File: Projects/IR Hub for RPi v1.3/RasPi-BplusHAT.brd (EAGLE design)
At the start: 65 x 56 mm, 37 parts, among them SW1 SPST_TACT-KMR2, SW2 SPST_TACT-KMR2, SW3 SPST_TACT-KMR2, T1 2N4401, T2 2N4401, T3 2N4401, T4 2N4401

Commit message: Revert "Revert "relocated IRRCV""
This reverts commit e9af4263ddd1cfc11cb1365f6dffa75911e4cf46.
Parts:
- added U$1, U$2: 74HC2G17-Q100, varshneya:SC-70-6L
- RUN: value (none) -> RST
- moved LED1-IR 25.2 mm to (8.00, 21.5)
- moved LED2-IR 25.2 mm to (8.00, 34.5)
- moved IRRCV 12.9 mm to (3.50, 12.5), turned to 270 degrees
- moved LED8-IR-RCV 10.1 mm to (13.5, 8.50), turned to 90 degrees
- moved R10 8.32 mm to (22.0, 4.00), turned to 180 degrees
- moved R8 7.16 mm to (13.5, 4.00), turned to 180 degrees
- moved T4 4.27 mm to (22.0, 14.0), turned to 180 degrees
- moved T3 4.00 mm to (15.0, 14.0), turned to 180 degrees
- moved T2 2.92 mm to (22.0, 27.0), turned to 0 degrees
- moved R11 2.69 mm to (22.0, 8.50), turned to 0 degrees
- moved R1 2.55 mm to (23.5, 35.0)
- moved R2 2.55 mm to (12.5, 35.0)
- moved R3 2.55 mm to (18.0, 35.0)
- moved C1 2.50 mm to (34.5, 12.0)
- moved R12 2.50 mm to (34.5, 20.0)
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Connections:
- new net N$12: C2.1, R13.1, SW2.1, SW2.3, U$1.3
- new net N$13: C3.1, R14.1, R15.1, U$2.3
- new net N$9: C1.1, R12.1, SW1.2, SW1.4, U$1.1
- net +3V3: now also U$1.5, U$2.5
- net GND: now also U$1.2, U$2.2
- net GPIO17: now also U$1.6; no longer C1.1, R12.1, SW1.2, SW1.4
- net GPIO27: now also U$1.4; no longer C2.1, R13.1, SW2.1, SW2.3
- net RST: now also U$2.4; no longer C3.1, R14.1, R15.1
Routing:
- net N$3: track 46.8 -> 10.2 mm
- net GPIO27: track 56.0 -> 29.2 mm
- net N$12: track 0.00 -> 26.4 mm, vias 0 -> 2
- net GPIO17: track 54.1 -> 29.7 mm
- net N$9: track 0.00 -> 23.4 mm, vias 0 -> 2
- net N$13: track 0.00 -> 17.7 mm
- net RST: track 67.3 -> 52.5 mm
- net +3V3: track 86.1 -> 100.4 mm
- net N$2: track 13.7 -> 27.5 mm
- net N$6: track 13.6 -> 24.9 mm
- net N$4: track 31.2 -> 22.5 mm
- net GPIO22: track 14.1 -> 22.7 mm, vias 2 -> 1
- net N$10: track 22.8 -> 15.6 mm
- net N$23: track 5.73 -> 12.3 mm
- net +5V: track 118.3 -> 124.3 mm
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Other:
- board text added: "HA Hub v1.3 July 2015"
- board text added: "Home Automation Hub v1.3"
- board text added: "Open Qbit Systems"
- board text added: "TODO 1. Check the Schmitt debouncing on breadboard 2. check the polarity of the IR LEDs 3. Check both ICs wrt 74HC/74LV/... for 3.3V DONE 1. Add schmitt buffers for all the push buttons (create part) 2. ELIMINATED - Verify the Watchdog circuit 3. ELIMINATED - Will RPi gpio go in a state to allow disabling WD? 4. Ensure long push for RESET push button (cap and resistor values) 5. Move Power LED to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"
- board text added: "openqbitsystems.blogspot.com"
- board text added: "|X>"
- board text removed: "HA Hub v3.0 July 10, 2015"
- board text removed: "Home Automation Hub v3.0"
- board text removed: "Qbit Devices"
- board text removed: "QbitDevices.wordpress.com"
- board text removed: "TODO 1. Add schmitt buffers for all the push buttons 2. check the polarity of the IR LEDs 3. Check both ICs wrt 74HC/74LV/... for 3.3V DONE 1. ELIMINATED - Verify the Watchdog circuit 2. ELIMINATED - Will RPi gpio go in a state to allow disabling WD? 3. Ensure long push for RESET push button (cap and resistor values) 4. Move Power LED to the Status LEDs area 5. check RUN location 6. Verify the IR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"
- board text removed: "|x>"

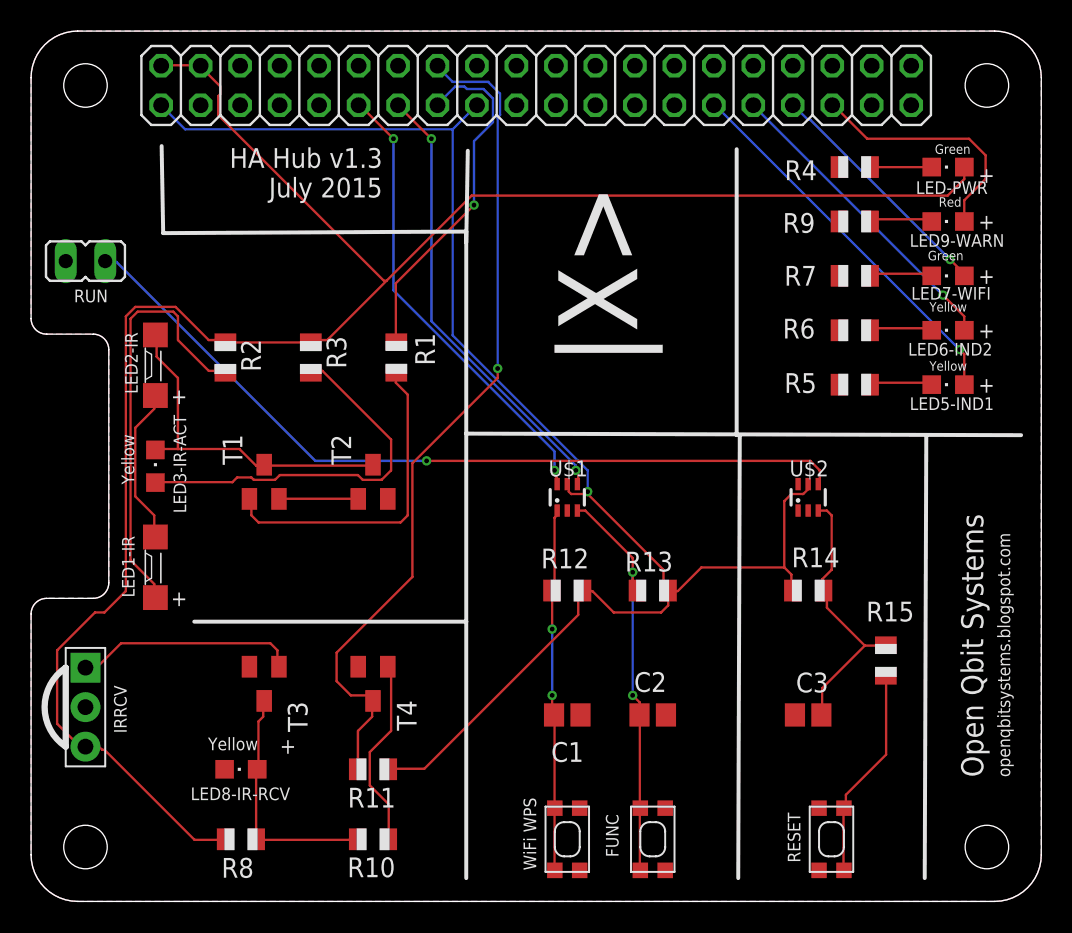
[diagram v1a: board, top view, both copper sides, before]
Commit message: minor teaks to silk, changed one LED to blue color
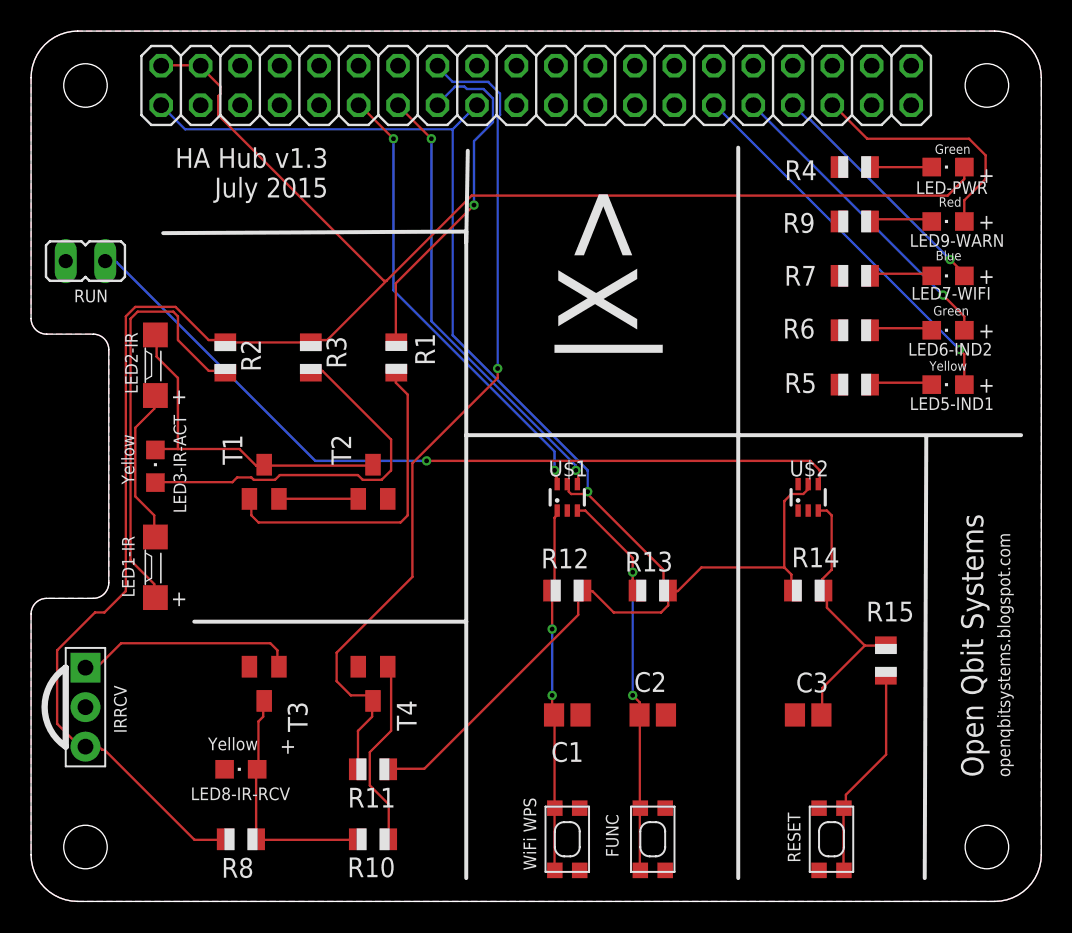
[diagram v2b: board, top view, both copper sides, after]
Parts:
- LED6-IND2: value Yellow -> Green
- LED7-WIFI: value Green -> Blue
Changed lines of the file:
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@@
 <circle x="61.5" y="52.5" radius="1.55" width="3.1" layer="42"/>
 <text x="61.27" y="7.99" size="1.4224" layer="25" rot="R90">Open Qbit Systems</text>
-<text x="22.61" y="48.47" size="1.27" layer="25" rot="R180">HA Hub v1.3
+<text x="19.11" y="48.47" size="1.27" layer="25" rot="R180">HA Hub v1.3
 July 2015</text>
 <wire x1="10.5" y1="18" x2="28" y2="18" width="0.254" layer="25"/>
-<wire x1="28" y1="43.1" x2="28" y2="30.1" width="0.254" layer="25"/>
-<wire x1="28" y1="30.1" x2="28" y2="18" width="0.254" layer="25"/>
+<wire x1="28" y1="43.1" x2="28" y2="30" width="0.254" layer="25"/>
+<wire x1="28" y1="30" x2="28" y2="18" width="0.254" layer="25"/>
 <wire x1="28" y1="18" x2="28" y2="1.5" width="0.254" layer="25"/>
 <wire x1="28" y1="43.1" x2="8.5" y2="43" width="0.254" layer="25"/>
@@
 <text x="32.5" y="2" size="0.8128" layer="25" rot="R90">WiFi WPS</text>
 <wire x1="28.1" y1="48.3" x2="28" y2="42.4" width="0.254" layer="25"/>
-<wire x1="45.4" y1="48.4" x2="45.4" y2="30" width="0.254" layer="25"/>
-<wire x1="63.7" y1="30" x2="28" y2="30.1" width="0.254" layer="25"/>
+<wire x1="45.5" y1="48.5" x2="45.5" y2="30" width="0.254" layer="25"/>
+<wire x1="63.7" y1="30" x2="28" y2="30" width="0.254" layer="25"/>
 <text x="-48.2222" y="19.964" size="1.016" layer="48">
 TODO
@@
 <text x="62" y="47.25" size="1.016" layer="21" rot="R180">+</text>
 <text x="16" y="9.5" size="1.016" layer="21">+</text>
-<wire x1="45.6" y1="29.9" x2="45.5" y2="1.5" width="0.254" layer="25"/>
+<wire x1="45.5" y1="29.9" x2="45.5" y2="1.5" width="0.254" layer="25"/>
 <text x="60" y="17" size="2.54" layer="26" rot="MR0">Open Qbit Systems</text>
 <text x="60" y="12.5" size="1.9304" layer="26" rot="MR0">openqbitsystems.blogspot.com</text>
@@
 <text x="63" y="8" size="0.8128" layer="25" rot="R90">openqbitsystems.blogspot.com</text>
 <text x="60" y="42" size="2.1844" layer="26" rot="MR0">Home Automation Hub v1.3</text>
-<wire x1="8.4" y1="48.6" x2="8.5" y2="43" width="0.254" layer="25"/>
 </plain>
 <attributes>
@@
 <attribute name="MPN" value="CRCW0805100RFKEA" x="53" y="33.25" size="1.778" layer="27" display="off"/>
 </element>
-<element name="LED6-IND2" library="led" package="CHIPLED_0805" value="Yellow" x="59" y="36.75" smashed="yes" rot="R90">
+<element name="LED6-IND2" library="led" package="CHIPLED_0805" value="Green" x="59" y="36.75" smashed="yes" rot="R90">
 <attribute name="NAME" x="56.43" y="35.12" size="0.8128" layer="25"/>
-<attribute name="VALUE" x="57.8" y="37.95" size="0.6096" layer="25"/>
-<attribute name="OC_NEWARK" value="95W3804" x="59" y="36.75" size="1.778" layer="27" rot="R90" display="off"/>
+<attribute name="VALUE" x="58.05" y="37.7" size="0.6096" layer="25"/>
+<attribute name="OC_NEWARK" value="95W3800" x="59" y="36.75" size="1.778" layer="27" rot="R90" display="off"/>
 <attribute name="MF" value="" x="59" y="36.75" size="1.778" layer="27" rot="R90" display="off"/>
-<attribute name="MPN" value="150080YS75000" x="59" y="36.75" size="1.778" layer="27" rot="R90" display="off"/>
+<attribute name="MPN" value="150080GS75000" x="59" y="36.75" size="1.778" layer="27" rot="R90" display="off"/>
 </element>
 <element name="R6" library="adafruit" package="R0805" value="100Ohm" x="53" y="36.75" smashed="yes">
@@
 <attribute name="MPN" value="CRCW0805100RFKEA" x="53" y="43.75" size="1.778" layer="27" display="off"/>
 </element>
-<element name="LED7-WIFI" library="led" package="CHIPLED_0805" value="Green" x="59" y="40.25" smashed="yes" rot="R90">
+<element name="LED7-WIFI" library="led" package="CHIPLED_0805" value="Blue" x="59" y="40.25" smashed="yes" rot="R90">
 <attribute name="NAME" x="56.63" y="38.72" size="0.8128" layer="25"/>
-<attribute name="VALUE" x="57.7" y="41.25" size="0.6096" layer="25"/>
-<attribute name="OC_NEWARK" value="95W3800" x="59" y="40.25" size="1.778" layer="27" rot="R90" display="off"/>
+<attribute name="VALUE" x="58.2" y="41.25" size="0.6096" layer="25"/>
+<attribute name="OC_NEWARK" value="95W3799" x="59" y="40.25" size="1.778" layer="27" rot="R90" display="off"/>
 <attribute name="MF" value="" x="59" y="40.25" size="1.778" layer="27" rot="R90" display="off"/>
-<attribute name="MPN" value="150080GS75000" x="59" y="40.25" size="1.778" layer="27" rot="R90" display="off"/>
+<attribute name="MPN" value="150080BS75000" x="59" y="40.25" size="1.778" layer="27" rot="R90" display="off"/>
 </element>
 <element name="R7" library="adafruit" package="R0805" value="100Ohm" x="53" y="40.25" smashed="yes">
@@
 <element name="R14" library="adafruit" package="R0805" value="1M" x="50" y="20" smashed="yes" rot="R180">
 <attribute name="MF" value="VISHAY/DALE" x="50" y="20" size="1.778" layer="27" rot="R180" display="off"/>
-<attribute name="MPN" value="CRCW080510K0FKEA" x="50" y="20" size="1.778" layer="27" rot="R180" display="off"/>
-<attribute name="OC_NEWARK" value="52K9795" x="50" y="20" size="1.778" layer="27" rot="R180" display="off"/>
+<attribute name="MPN" value="CRCW08051M00FKEA" x="50" y="20" size="1.778" layer="27" rot="R180" display="off"/>
+<attribute name="OC_NEWARK" value="52K9759" x="50" y="20" size="1.778" layer="27" rot="R180" display="off"/>
 <attribute name="NAME" x="48.938" y="21.5" size="1.27" layer="25"/>
 </element>
@@
 </element>
 <element name="R15" library="adafruit" package="R0805" value="100K" x="55" y="15.5" smashed="yes" rot="R270">
-<attribute name="OC_NEWARK" value="52K9795" x="55" y="15.5" size="1.016" layer="27" rot="R270" display="off"/>
+<attribute name="OC_NEWARK" value="52K9808" x="55" y="15.5" size="1.016" layer="27" rot="R270" display="off"/>
 <attribute name="MF" value="VISHAY/DALE" x="55" y="15.5" size="1.016" layer="27" rot="R270" display="off"/>
-<attribute name="MPN" value="CRCW080510K0FKEA" x="55" y="15.5" size="1.016" layer="27" rot="R270" display="off"/>
+<attribute name="MPN" value="CRCW0805100KFKEA" x="55" y="15.5" size="1.016" layer="27" rot="R270" display="off"/>
 <attribute name="NAME" x="53.738" y="18.016" size="1.27" layer="25"/>
 </element>
 <element name="U$1" library="varshneya" package="SC-70-6L" value="74HC2G17-Q100" x="34.5" y="26" smashed="yes">
 <attribute name="NAME" x="33.3" y="27.35" size="1.016" layer="25"/>
+<attribute name="OC_NEWARK" value="71R2196" x="34.5" y="26" size="1.778" layer="27" display="off"/>
+<attribute name="MF" value="" x="34.5" y="26" size="1.778" layer="27" display="off"/>
+<attribute name="MPN" value="74HC2G17GW,125" x="34.5" y="26" size="1.778" layer="27" display="off"/>
 </element>
 <element name="U$2" library="varshneya" package="SC-70-6L" value="74HC2G17-Q100" x="50" y="26" smashed="yes">
 <attribute name="NAME" x="48.8" y="27.35" size="1.016" layer="25"/>
+<attribute name="OC_NEWARK" value="71R2196" x="50" y="26" size="1.778" layer="27" display="off"/>
+<attribute name="MF" value="" x="50" y="26" size="1.778" layer="27" display="off"/>
+<attribute name="MPN" value="74HC2G17GW,125" x="50" y="26" size="1.778" layer="27" display="off"/>
 </element>
 </elements>

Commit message: near final version - checkpoint
Pending AIs -
check polarity of the IR LEDs
check the buffer circuit on breadboard
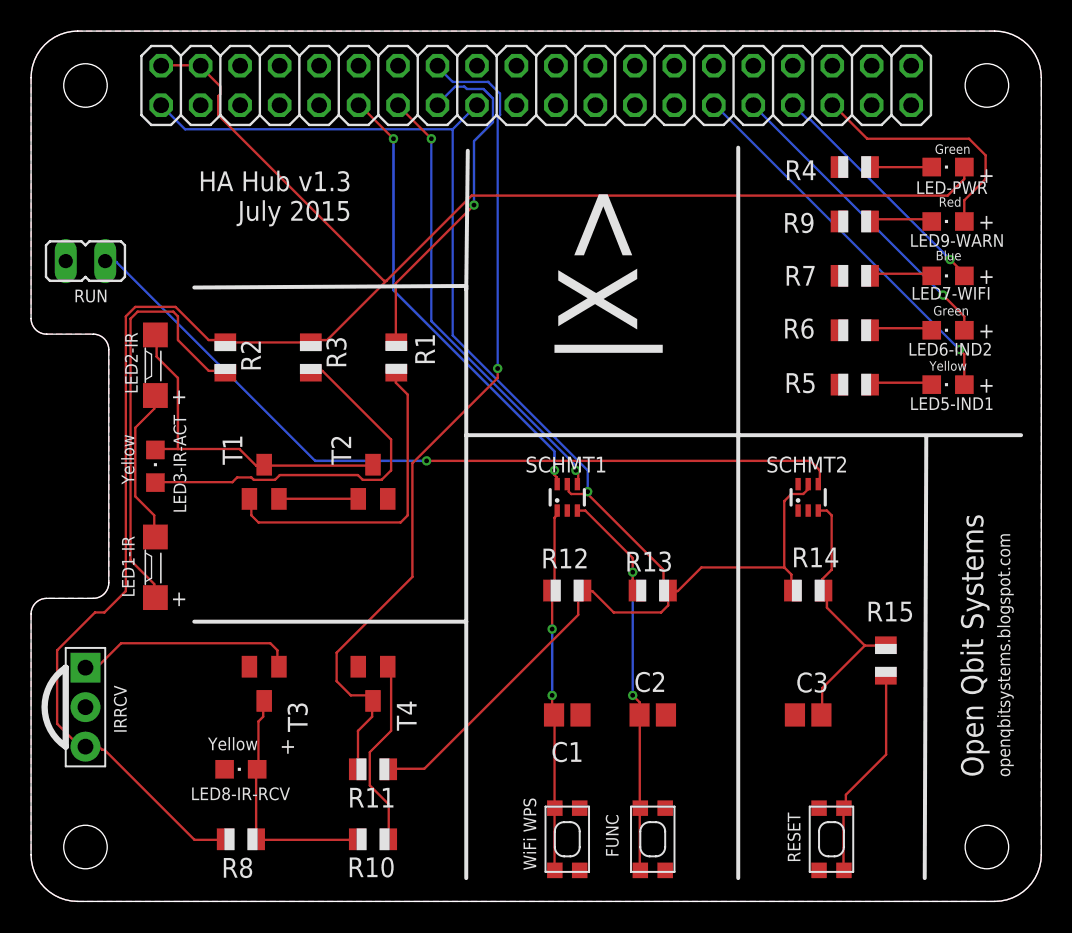
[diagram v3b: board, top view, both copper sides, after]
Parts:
- renumbered U$1 to SCHMT1, U$2 to SCHMT2
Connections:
- net GND: now also SCHMT2.1
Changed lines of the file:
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@@
 <circle x="61.5" y="52.5" radius="1.55" width="3.1" layer="42"/>
 <text x="61.27" y="7.99" size="1.4224" layer="25" rot="R90">Open Qbit Systems</text>
-<text x="19.11" y="48.47" size="1.27" layer="25" rot="R180">HA Hub v1.3
+<text x="20.61" y="46.97" size="1.27" layer="25" rot="R180">HA Hub v1.3
 July 2015</text>
 <wire x1="10.5" y1="18" x2="28" y2="18" width="0.254" layer="25"/>
-<wire x1="28" y1="43.1" x2="28" y2="30" width="0.254" layer="25"/>
+<wire x1="28" y1="39.6" x2="28" y2="39.4" width="0.254" layer="25"/>
+<wire x1="28" y1="39.4" x2="28" y2="30" width="0.254" layer="25"/>
 <wire x1="28" y1="30" x2="28" y2="18" width="0.254" layer="25"/>
 <wire x1="28" y1="18" x2="28" y2="1.5" width="0.254" layer="25"/>
-<wire x1="28" y1="43.1" x2="8.5" y2="43" width="0.254" layer="25"/>
+<wire x1="28" y1="39.6" x2="10.5" y2="39.5" width="0.254" layer="25"/>
 <wire x1="57.6" y1="29.9" x2="57.5" y2="1.5" width="0.254" layer="25"/>
 <text x="49.5" y="2.5" size="0.8128" layer="25" rot="R90">RESET</text>
 <text x="37.8" y="2.85" size="0.8128" layer="25" rot="R90">FUNC</text>
 <text x="32.5" y="2" size="0.8128" layer="25" rot="R90">WiFi WPS</text>
-<wire x1="28.1" y1="48.3" x2="28" y2="42.4" width="0.254" layer="25"/>
+<wire x1="28.1" y1="48.3" x2="28" y2="39.4" width="0.254" layer="25"/>
 <wire x1="45.5" y1="48.5" x2="45.5" y2="30" width="0.254" layer="25"/>
 <wire x1="63.7" y1="30" x2="28" y2="30" width="0.254" layer="25"/>
@@
 <attribute name="NAME" x="53.738" y="18.016" size="1.27" layer="25"/>
 </element>
-<element name="U$1" library="varshneya" package="SC-70-6L" value="74HC2G17-Q100" x="34.5" y="26" smashed="yes">
-<attribute name="NAME" x="33.3" y="27.35" size="1.016" layer="25"/>
+<element name="SCHMT1" library="varshneya" package="SC-70-6L" value="74HC2G17-Q100" x="34.5" y="26" smashed="yes">
+<attribute name="NAME" x="31.8" y="27.6" size="1.016" layer="25"/>
 <attribute name="OC_NEWARK" value="71R2196" x="34.5" y="26" size="1.778" layer="27" display="off"/>
 <attribute name="MF" value="" x="34.5" y="26" size="1.778" layer="27" display="off"/>
 <attribute name="MPN" value="74HC2G17GW,125" x="34.5" y="26" size="1.778" layer="27" display="off"/>
 </element>
-<element name="U$2" library="varshneya" package="SC-70-6L" value="74HC2G17-Q100" x="50" y="26" smashed="yes">
-<attribute name="NAME" x="48.8" y="27.35" size="1.016" layer="25"/>
+<element name="SCHMT2" library="varshneya" package="SC-70-6L" value="74HC2G17-Q100" x="50" y="26" smashed="yes">
+<attribute name="NAME" x="47.3" y="27.6" size="1.016" layer="25"/>
 <attribute name="OC_NEWARK" value="71R2196" x="50" y="26" size="1.778" layer="27" display="off"/>
 <attribute name="MF" value="" x="50" y="26" size="1.778" layer="27" display="off"/>
@@
 <contactref element="SW1" pad="1"/>
 <contactref element="SW1" pad="3"/>
-<contactref element="U$1" pad="2"/>
-<contactref element="U$2" pad="2"/>
+<contactref element="SCHMT1" pad="2"/>
+<contactref element="SCHMT2" pad="2"/>
+<contactref element="SCHMT2" pad="1"/>
 </signal>
 <signal name="+3V3">
@@
 <contactref element="R14" pad="2"/>
 <contactref element="R12" pad="2"/>
-<contactref element="U$1" pad="5"/>
-<contactref element="U$2" pad="5"/>
+<contactref element="SCHMT1" pad="5"/>
+<contactref element="SCHMT2" pad="5"/>
 <wire x1="9.906" y1="49.6824" x2="8.382" y2="51.2064" width="0.1524" layer="16"/>
 <wire x1="27.1272" y1="49.6824" x2="9.906" y2="49.6824" width="0.1524" layer="16"/>
@@
 <signal name="GPIO17">
 <contactref element="HDR1" pad="11"/>
-<contactref element="U$1" pad="6"/>
+<contactref element="SCHMT1" pad="6"/>
 <wire x1="33.8328" y1="27.2796" x2="33.8328" y2="26.9748" width="0.1524" layer="1"/>
 <wire x1="33.6804" y1="27.432" x2="33.8328" y2="27.2796" width="0.1524" layer="1"/>
@@
 <signal name="GPIO27">
 <contactref element="HDR1" pad="13"/>
-<contactref element="U$1" pad="4"/>
+<contactref element="SCHMT1" pad="4"/>
 <wire x1="35.2044" y1="27.5844" x2="35.2044" y2="26.9748" width="0.1524" layer="1"/>
 <wire x1="35.052" y1="27.7368" x2="35.2044" y2="27.5844" width="0.1524" layer="1"/>
@@
 <signal name="RST">
 <contactref element="RUN" pad="2"/>
-<contactref element="U$2" pad="4"/>
+<contactref element="SCHMT2" pad="4"/>
 <wire x1="50.7492" y1="27.7368" x2="50.7492" y2="26.9748" width="0.1524" layer="1"/>
 <wire x1="50.1396" y1="28.3464" x2="50.7492" y2="27.7368" width="0.1524" layer="1"/>
@@
 <contactref element="C1" pad="1"/>
 <contactref element="R12" pad="1"/>
-<contactref element="U$1" pad="1"/>
+<contactref element="SCHMT1" pad="1"/>
 <wire x1="33.8328" y1="24.8412" x2="33.8328" y2="25.146" width="0.1524" layer="1"/>
 <wire x1="33.6804" y1="24.6888" x2="33.8328" y2="24.8412" width="0.1524" layer="1"/>
@@
 <contactref element="C2" pad="1"/>
 <contactref element="R13" pad="1"/>
-<contactref element="U$1" pad="3"/>
+<contactref element="SCHMT1" pad="3"/>
 <wire x1="35.6616" y1="25.146" x2="35.2044" y2="25.146" width="0.1524" layer="1"/>
 <wire x1="38.7096" y1="22.098" x2="35.6616" y2="25.146" width="0.1524" layer="1"/>
@@
 <signal name="N$13">
 <contactref element="R15" pad="1"/>
-<contactref element="U$2" pad="3"/>
+<contactref element="SCHMT2" pad="3"/>
 <contactref element="R14" pad="1"/>
 <contactref element="C3" pad="1"/>
